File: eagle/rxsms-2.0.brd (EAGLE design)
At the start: 160 x 100 mm, 147 parts, among them Q1 opt, Q10 BSS123, Q11 BSS123, Q12 BSS123, Q2 BSS123, Q3 BSS123, Q4 BSS123, Q5 BSS123, Q6 BSS123, Q7 BSS123, Q8 BSS123, Q9 BSS123, T1 SMS_IP67, T10 SWITCH_LED, T2 SMS_IP67, T3 SWITCH_LED, T4 SMS_IP67, T5 SMS_IP67, T6 SWITCH_LED, T7 SWITCH_LED, T8 SWITCH_LED, T9 SMS_IP67, U1 MAX3232ESE, U2 XMEGA-A4UTQFP, U3 TSR_1-2450, U4 LM1117, U5 TMV_0505EN, U6 ADUM3160, U7 TPS73125, U8 NUP2202W1, X1 PN61729-S, X5 RLP2-200-500

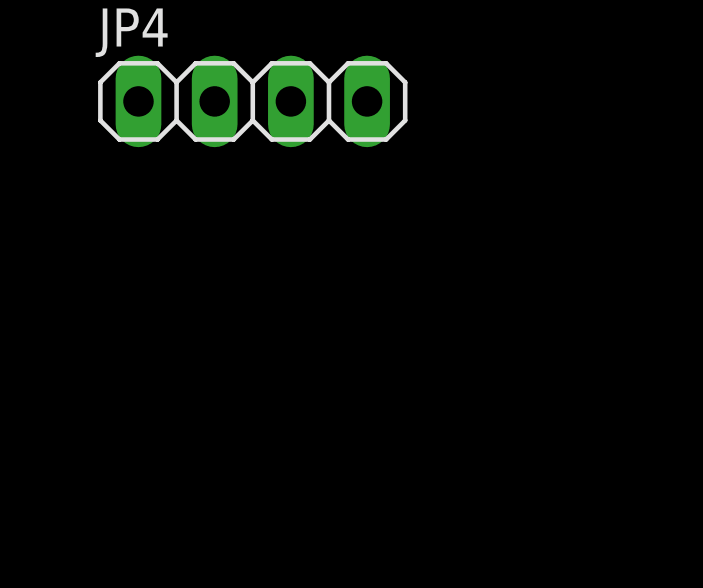
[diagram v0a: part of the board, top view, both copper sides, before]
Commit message: add pinheaders for reserved ADC and GPIO pins
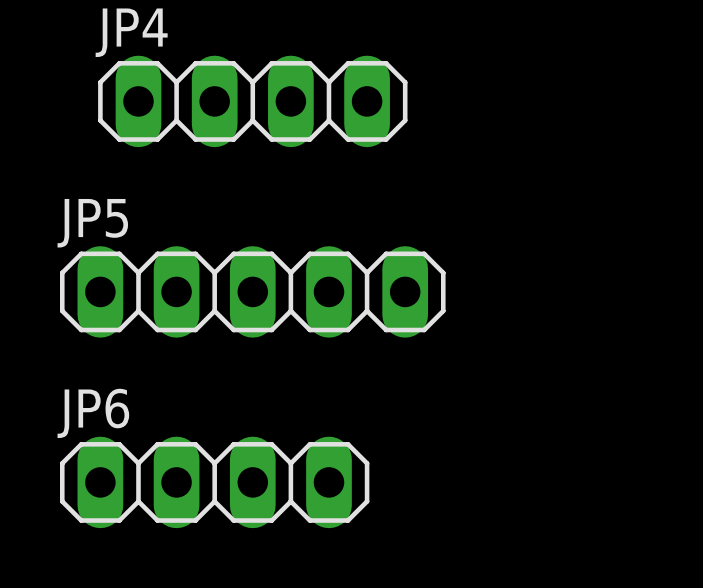
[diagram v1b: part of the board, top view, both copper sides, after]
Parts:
- added JP5: (no value), pinhead:1X05
- added JP6: (no value), pinhead:1X04
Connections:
- new net N$33: JP6.2, U2.28
- new net N$36: JP6.3, U2.29
- new net RESERVED_ADC_0: U2.44
- new net RESERVED_ADC_1: U2.1
- net +3V3: now also JP5.1, JP6.1
- net GND: now also JP5.5, JP6.4
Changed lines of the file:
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@@
 <element name="JP3" library="pinhead" package="1X04" value="" x="-420.37" y="-471.17"/>
 <element name="JP4" library="pinhead" package="1X04" value="" x="-420.37" y="-477.52"/>
+<element name="JP5" library="pinhead" package="1X05" value="" x="-420.37" y="-483.87"/>
+<element name="JP6" library="pinhead" package="1X04" value="" x="-421.64" y="-490.22"/>
 </elements>
 <signals>
@@
 <contactref element="JP3" pad="4"/>
 <contactref element="JP4" pad="4"/>
-<wire x1="-282.21" y1="-298.45" x2="-287.29" y2="-298.45" width="0" layer="19" extent="1-1"/>
-<wire x1="-266.7" y1="-293.37" x2="-282.21" y2="-298.45" width="0" layer="19" extent="1-1"/>
-<wire x1="-266.7" y1="-290.83" x2="-266.7" y2="-293.37" width="0" layer="19" extent="1-1"/>
-<wire x1="-266.7" y1="-281.94" x2="-266.7" y2="-290.83" width="0" layer="19" extent="1-1"/>
-<wire x1="-287.075" y1="-272.63" x2="-266.7" y2="-281.94" width="0" layer="19" extent="1-1"/>
-<wire x1="-287.075" y1="-258.43" x2="-287.075" y2="-272.63" width="0" layer="19" extent="1-1"/>
-<wire x1="-266.7" y1="-254" x2="-287.075" y2="-258.43" width="0" layer="19" extent="1-1"/>
-<wire x1="-266.7" y1="-251.46" x2="-266.7" y2="-254" width="0" layer="19" extent="1-1"/>
-<wire x1="-266.7" y1="-242.57" x2="-266.7" y2="-251.46" width="0" layer="19" extent="1-1"/>
-<wire x1="-266.7" y1="-240.03" x2="-266.7" y2="-242.57" width="0" layer="19" extent="1-1"/>
+<contactref element="JP5" pad="5"/>
+<contactref element="JP6" pad="4"/>
+<wire x1="-266.7" y1="-242.57" x2="-266.7" y2="-240.03" width="0" layer="19" extent="1-1"/>
+<wire x1="-266.7" y1="-251.46" x2="-266.7" y2="-242.57" width="0" layer="19" extent="1-1"/>
+<wire x1="-266.7" y1="-254" x2="-266.7" y2="-251.46" width="0" layer="19" extent="1-1"/>
+<wire x1="-287.075" y1="-258.43" x2="-266.7" y2="-254" width="0" layer="19" extent="1-1"/>
+<wire x1="-287.075" y1="-272.63" x2="-287.075" y2="-258.43" width="0" layer="19" extent="1-1"/>
+<wire x1="-266.7" y1="-281.94" x2="-287.075" y2="-272.63" width="0" layer="19" extent="1-1"/>
+<wire x1="-266.7" y1="-290.83" x2="-266.7" y2="-281.94" width="0" layer="19" extent="1-1"/>
+<wire x1="-266.7" y1="-293.37" x2="-266.7" y2="-290.83" width="0" layer="19" extent="1-1"/>
+<wire x1="-282.21" y1="-298.45" x2="-266.7" y2="-293.37" width="0" layer="19" extent="1-1"/>
+<wire x1="-287.29" y1="-298.45" x2="-282.21" y2="-298.45" width="0" layer="19" extent="1-1"/>
 <wire x1="-283.972" y1="-222.25" x2="-266.7" y2="-240.03" width="0" layer="19" extent="1-1"/>
 <wire x1="-266.7" y1="-327.66" x2="-282.21" y2="-298.45" width="0" layer="19" extent="1-1"/>
@@
 <wire x1="-416.56" y1="-471.17" x2="-408.62" y2="-463.55" width="0" layer="19" extent="1-1"/>
 <wire x1="-416.56" y1="-477.52" x2="-416.56" y2="-471.17" width="0" layer="19" extent="1-1"/>
+<wire x1="-415.29" y1="-483.87" x2="-416.56" y2="-477.52" width="0" layer="19" extent="1-1"/>
+<wire x1="-417.83" y1="-490.22" x2="-415.29" y2="-483.87" width="0" layer="19" extent="1-1"/>
 <wire x1="-280.035" y1="-167.1066" x2="-283.972" y2="-222.25" width="0" layer="19" extent="1-1"/>
 <wire x1="-280.035" y1="-118.8466" x2="-280.035" y2="-167.1066" width="0" layer="19" extent="1-1"/>
@@
 <wire x1="-178.07" y1="153.67" x2="-190.24" y2="139.98" width="0" layer="19" extent="1-1"/>
 <wire x1="-178.07" y1="158.75" x2="-178.07" y2="153.67" width="0" layer="19" extent="1-1"/>
-<wire x1="-169.545" y1="-221.46" x2="-178.07" y2="158.75" width="0" layer="19" extent="1-1"/>
+<wire x1="-169.545" y1="-221.46" x2="-266.7" y2="-240.03" width="0" layer="19" extent="1-1"/>
 <wire x1="-164.465" y1="-221.46" x2="-169.545" y2="-221.46" width="0" layer="19" extent="1-1"/>
 <wire x1="-129.81" y1="-194.31" x2="-164.465" y2="-221.46" width="0" layer="19" extent="1-1"/>
@@
 <contactref element="JP3" pad="1"/>
 <contactref element="JP4" pad="1"/>
+<contactref element="JP5" pad="1"/>
+<contactref element="JP6" pad="1"/>
 <wire x1="-122.24" y1="-156.21" x2="-105.41" y2="-134.62" width="0" layer="19" extent="1-1"/>
 <wire x1="-122.24" y1="-162.56" x2="-122.24" y2="-156.21" width="0" layer="19" extent="1-1"/>
@@
 <wire x1="-89.23" y1="28.66" x2="-93.43" y2="20.46" width="0" layer="19" extent="1-1"/>
 <wire x1="-81.83" y1="25.26" x2="-89.23" y2="28.66" width="0" layer="19" extent="1-1"/>
-<wire x1="-180.07" y1="158.75" x2="-170.815" y2="-221.46" width="0" layer="19" extent="1-1"/>
-<wire x1="-180.07" y1="153.67" x2="-180.07" y2="158.75" width="0" layer="19" extent="1-1"/>
-<wire x1="-187.96" y1="147.28" x2="-180.07" y2="153.67" width="0" layer="19" extent="1-1"/>
-<wire x1="-273.37" y1="-82.55" x2="-187.96" y2="147.28" width="0" layer="19" extent="1-1"/>
-<wire x1="-273.37" y1="-88.9" x2="-273.37" y2="-82.55" width="0" layer="19" extent="1-1"/>
-<wire x1="-265.75" y1="-114.3" x2="-273.37" y2="-88.9" width="0" layer="19" extent="1-1"/>
-<wire x1="-273.37" y1="-123.19" x2="-265.75" y2="-114.3" width="0" layer="19" extent="1-1"/>
-<wire x1="-282.575" y1="-118.8466" x2="-273.37" y2="-123.19" width="0" layer="19" extent="1-1"/>
-<wire x1="-283.845" y1="-118.8466" x2="-282.575" y2="-118.8466" width="0" layer="19" extent="1-1"/>
-<wire x1="-283.53" y1="-129.54" x2="-283.845" y2="-118.8466" width="0" layer="19" extent="1-1"/>
-<wire x1="-283.845" y1="-167.1066" x2="-283.53" y2="-129.54" width="0" layer="19" extent="1-1"/>
-<wire x1="-282.575" y1="-167.1066" x2="-283.845" y2="-167.1066" width="0" layer="19" extent="1-1"/>
-<wire x1="-274.64" y1="-177.8" x2="-282.575" y2="-167.1066" width="0" layer="19" extent="1-1"/>
+<wire x1="-274.64" y1="-177.8" x2="-170.815" y2="-221.46" width="0" layer="19" extent="1-1"/>
+<wire x1="-282.575" y1="-167.1066" x2="-274.64" y2="-177.8" width="0" layer="19" extent="1-1"/>
+<wire x1="-283.845" y1="-167.1066" x2="-282.575" y2="-167.1066" width="0" layer="19" extent="1-1"/>
+<wire x1="-283.53" y1="-129.54" x2="-282.575" y2="-167.1066" width="0" layer="19" extent="1-1"/>
+<wire x1="-283.845" y1="-118.8466" x2="-283.53" y2="-129.54" width="0" layer="19" extent="1-1"/>
+<wire x1="-282.575" y1="-118.8466" x2="-283.845" y2="-118.8466" width="0" layer="19" extent="1-1"/>
+<wire x1="-273.37" y1="-123.19" x2="-282.575" y2="-118.8466" width="0" layer="19" extent="1-1"/>
+<wire x1="-265.75" y1="-114.3" x2="-273.37" y2="-123.19" width="0" layer="19" extent="1-1"/>
+<wire x1="-273.37" y1="-88.9" x2="-265.75" y2="-114.3" width="0" layer="19" extent="1-1"/>
+<wire x1="-273.37" y1="-82.55" x2="-273.37" y2="-88.9" width="0" layer="19" extent="1-1"/>
+<wire x1="-187.96" y1="147.28" x2="-89.23" y2="28.66" width="0" layer="19" extent="1-1"/>
+<wire x1="-180.07" y1="153.67" x2="-187.96" y2="147.28" width="0" layer="19" extent="1-1"/>
+<wire x1="-180.07" y1="158.75" x2="-180.07" y2="153.67" width="0" layer="19" extent="1-1"/>
 <wire x1="-307.02" y1="-360.68" x2="-274.64" y2="-177.8" width="0" layer="19" extent="1-1"/>
 <wire x1="-305.12" y1="-381" x2="-307.02" y2="-360.68" width="0" layer="19" extent="1-1"/>
@@
 <wire x1="-424.18" y1="-471.17" x2="-305.12" y2="-393.7" width="0" layer="19" extent="1-1"/>
 <wire x1="-424.18" y1="-477.52" x2="-424.18" y2="-471.17" width="0" layer="19" extent="1-1"/>
+<wire x1="-425.45" y1="-483.87" x2="-424.18" y2="-477.52" width="0" layer="19" extent="1-1"/>
+<wire x1="-425.45" y1="-490.22" x2="-425.45" y2="-483.87" width="0" layer="19" extent="1-1"/>
 </signal>
 <signal name="N$11">
@@
 <contactref element="JP3" pad="3"/>
 </signal>
+<signal name="RESERVED_ADC_0">
+<contactref element="U2" pad="44"/>
+</signal>
+<signal name="RESERVED_ADC_1">
+<contactref element="U2" pad="1"/>
+</signal>
+<signal name="N$33">
+<contactref element="U2" pad="28"/>
+<contactref element="JP6" pad="2"/>
+<wire x1="-93.43" y1="22.86" x2="-422.91" y2="-490.22" width="0" layer="19" extent="1-1"/>
+</signal>
+<signal name="N$36">
+<contactref element="U2" pad="29"/>
+<contactref element="JP6" pad="3"/>
+<wire x1="-93.43" y1="22.06" x2="-420.37" y2="-490.22" width="0" layer="19" extent="1-1"/>
+</signal>
 </signals>

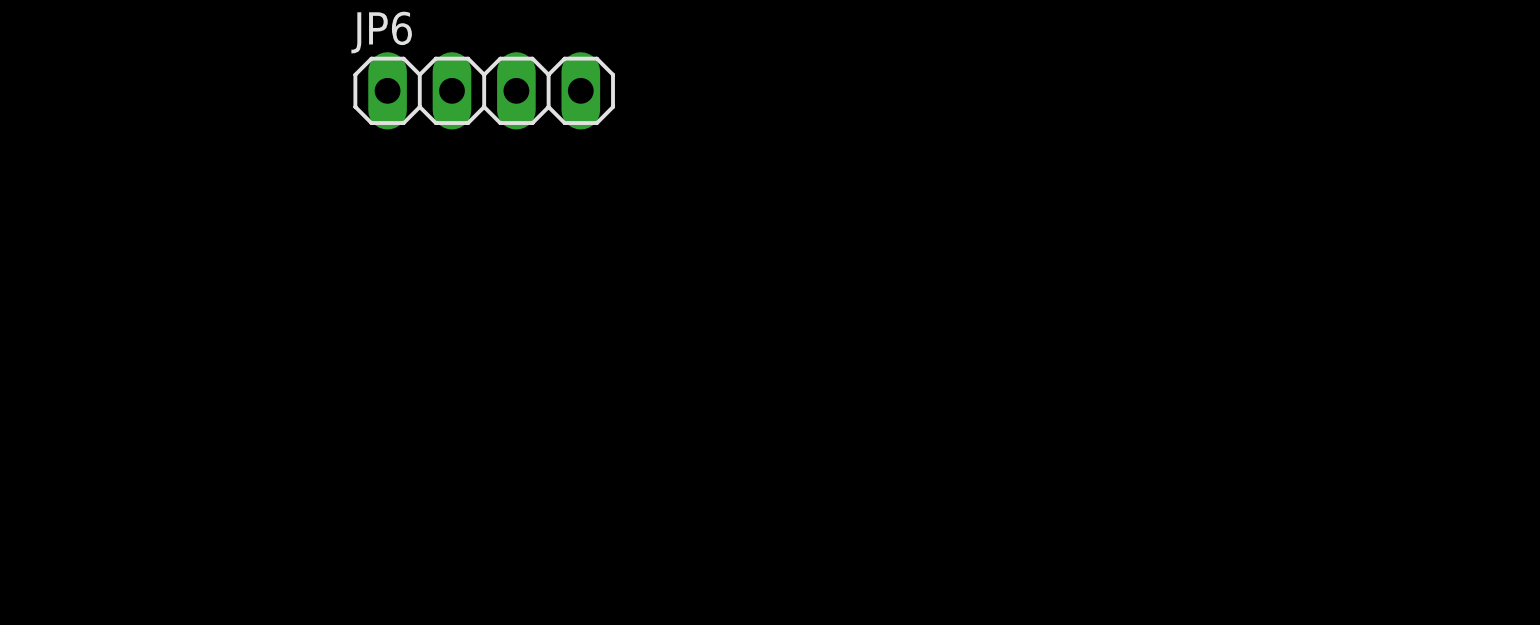
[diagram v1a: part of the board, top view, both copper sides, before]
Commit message: add power supply connectors
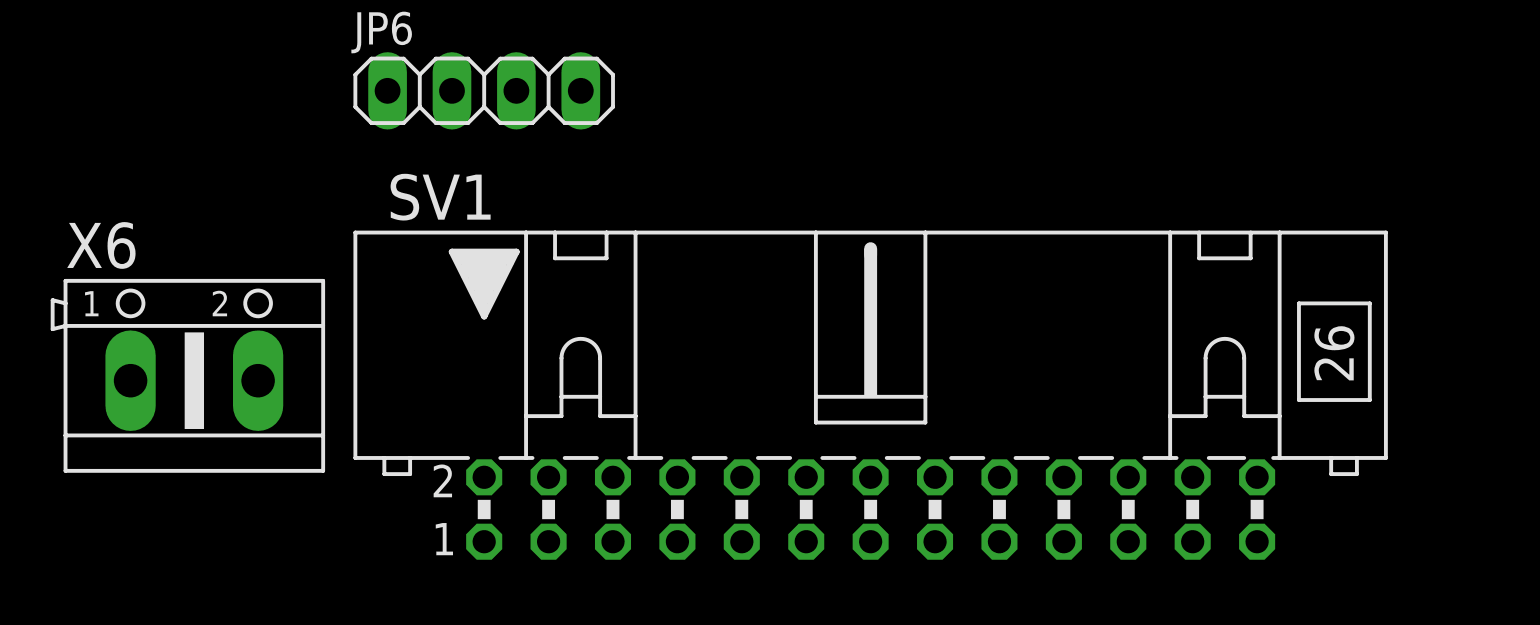
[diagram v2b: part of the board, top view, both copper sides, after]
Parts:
- added SV1: (no value), con-harting-ml:ML26L
- added X6: (no value), con-ptr500:AK500/2
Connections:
- new net N$67: SV1.10, SV1.12, SV1.14, SV1.4, SV1.6, SV1.8
- new net N$69: SV1.11, SV1.13, SV1.3, SV1.5, SV1.7, SV1.9
- net +28V_SUPPLY: now also SV1.15, SV1.16, SV1.17, SV1.18, SV1.19, SV1.20, SV1.21, SV1.22, SV1.23, SV1.24, SV1.25, SV1.26, X6.1
- net GND: now also X6.2
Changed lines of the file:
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@@
 <element name="JP5" library="pinhead" package="1X05" value="" x="-420.37" y="-483.87"/>
 <element name="JP6" library="pinhead" package="1X04" value="" x="-421.64" y="-490.22"/>
+<element name="SV1" library="con-harting-ml" package="ML26L" value="" x="-406.4" y="-506.73">
+<attribute name="OC_NEWARK" value="unknown" x="-406.4" y="-506.73" size="1.778" layer="27" display="off"/>
+<attribute name="MPN" value="" x="-406.4" y="-506.73" size="1.778" layer="27" display="off"/>
+<attribute name="MF" value="" x="-406.4" y="-506.73" size="1.778" layer="27" display="off"/>
+<attribute name="OC_FARNELL" value="unknown" x="-406.4" y="-506.73" size="1.778" layer="27" display="off"/>
+</element>
+<element name="X6" library="con-ptr500" package="AK500/2" value="" x="-433.07" y="-501.65">
+<attribute name="OC_NEWARK" value="unknown" x="-433.07" y="-501.65" size="1.778" layer="27" display="off"/>
+<attribute name="MPN" value="" x="-433.07" y="-501.65" size="1.778" layer="27" display="off"/>
+<attribute name="MF" value="" x="-433.07" y="-501.65" size="1.778" layer="27" display="off"/>
+<attribute name="OC_FARNELL" value="unknown" x="-433.07" y="-501.65" size="1.778" layer="27" display="off"/>
+</element>
 </elements>
 <signals>
@@
 <contactref element="JP5" pad="5"/>
 <contactref element="JP6" pad="4"/>
+<contactref element="X6" pad="2"/>
 <wire x1="-266.7" y1="-242.57" x2="-266.7" y2="-240.03" width="0" layer="19" extent="1-1"/>
 <wire x1="-266.7" y1="-251.46" x2="-266.7" y2="-242.57" width="0" layer="19" extent="1-1"/>
@@
 <wire x1="-415.29" y1="-483.87" x2="-416.56" y2="-477.52" width="0" layer="19" extent="1-1"/>
 <wire x1="-417.83" y1="-490.22" x2="-415.29" y2="-483.87" width="0" layer="19" extent="1-1"/>
+<wire x1="-430.5554" y1="-501.65" x2="-417.83" y2="-490.22" width="0" layer="19" extent="1-1"/>
 <wire x1="-280.035" y1="-167.1066" x2="-283.972" y2="-222.25" width="0" layer="19" extent="1-1"/>
 <wire x1="-280.035" y1="-118.8466" x2="-280.035" y2="-167.1066" width="0" layer="19" extent="1-1"/>
@@
 <contactref element="U$6" pad="TAB"/>
 <contactref element="C12" pad="1"/>
-<wire x1="-154.94" y1="-119.68" x2="-101.33" y2="-55.88" width="0" layer="19" extent="1-1"/>
+<contactref element="SV1" pad="16"/>
+<contactref element="SV1" pad="26"/>
+<contactref element="SV1" pad="18"/>
+<contactref element="SV1" pad="20"/>
+<contactref element="SV1" pad="22"/>
+<contactref element="SV1" pad="24"/>
+<contactref element="SV1" pad="25"/>
+<contactref element="SV1" pad="15"/>
+<contactref element="SV1" pad="17"/>
+<contactref element="SV1" pad="19"/>
+<contactref element="SV1" pad="21"/>
+<contactref element="SV1" pad="23"/>
+<contactref element="X6" pad="1"/>
+<wire x1="-403.86" y1="-505.46" x2="-435.5846" y2="-501.65" width="0" layer="19" extent="1-1"/>
+<wire x1="-403.86" y1="-508" x2="-403.86" y2="-505.46" width="0" layer="19" extent="1-1"/>
+<wire x1="-401.32" y1="-508" x2="-403.86" y2="-508" width="0" layer="19" extent="1-1"/>
+<wire x1="-401.32" y1="-505.46" x2="-403.86" y2="-505.46" width="0" layer="19" extent="1-1"/>
+<wire x1="-398.78" y1="-508" x2="-401.32" y2="-508" width="0" layer="19" extent="1-1"/>
+<wire x1="-398.78" y1="-505.46" x2="-401.32" y2="-505.46" width="0" layer="19" extent="1-1"/>
+<wire x1="-396.24" y1="-508" x2="-398.78" y2="-508" width="0" layer="19" extent="1-1"/>
+<wire x1="-396.24" y1="-505.46" x2="-398.78" y2="-505.46" width="0" layer="19" extent="1-1"/>
+<wire x1="-393.7" y1="-508" x2="-396.24" y2="-508" width="0" layer="19" extent="1-1"/>
+<wire x1="-393.7" y1="-505.46" x2="-396.24" y2="-505.46" width="0" layer="19" extent="1-1"/>
+<wire x1="-391.16" y1="-508" x2="-393.7" y2="-508" width="0" layer="19" extent="1-1"/>
+<wire x1="-391.16" y1="-505.46" x2="-393.7" y2="-505.46" width="0" layer="19" extent="1-1"/>
+<wire x1="-154.94" y1="-119.68" x2="-391.16" y2="-505.46" width="0" layer="19" extent="1-1"/>
+<wire x1="-101.33" y1="-55.88" x2="-154.94" y2="-119.68" width="0" layer="19" extent="1-1"/>
 </signal>
 <signal name="N$25">
@@
 <wire x1="-93.43" y1="22.06" x2="-420.37" y2="-490.22" width="0" layer="19" extent="1-1"/>
 </signal>
+<signal name="N$67">
+<contactref element="SV1" pad="4"/>
+<contactref element="SV1" pad="14"/>
+<contactref element="SV1" pad="12"/>
+<contactref element="SV1" pad="10"/>
+<contactref element="SV1" pad="8"/>
+<contactref element="SV1" pad="6"/>
+<wire x1="-416.56" y1="-505.46" x2="-419.1" y2="-505.46" width="0" layer="19" extent="1-1"/>
+<wire x1="-414.02" y1="-505.46" x2="-416.56" y2="-505.46" width="0" layer="19" extent="1-1"/>
+<wire x1="-411.48" y1="-505.46" x2="-414.02" y2="-505.46" width="0" layer="19" extent="1-1"/>
+<wire x1="-408.94" y1="-505.46" x2="-411.48" y2="-505.46" width="0" layer="19" extent="1-1"/>
+<wire x1="-406.4" y1="-505.46" x2="-408.94" y2="-505.46" width="0" layer="19" extent="1-1"/>
+</signal>
+<signal name="N$69">
+<contactref element="SV1" pad="13"/>
+<contactref element="SV1" pad="3"/>
+<contactref element="SV1" pad="5"/>
+<contactref element="SV1" pad="7"/>
+<contactref element="SV1" pad="9"/>
+<contactref element="SV1" pad="11"/>
+<wire x1="-416.56" y1="-508" x2="-419.1" y2="-508" width="0" layer="19" extent="1-1"/>
+<wire x1="-414.02" y1="-508" x2="-416.56" y2="-508" width="0" layer="19" extent="1-1"/>
+<wire x1="-411.48" y1="-508" x2="-414.02" y2="-508" width="0" layer="19" extent="1-1"/>
+<wire x1="-408.94" y1="-508" x2="-411.48" y2="-508" width="0" layer="19" extent="1-1"/>
+<wire x1="-406.4" y1="-508" x2="-408.94" y2="-508" width="0" layer="19" extent="1-1"/>
+</signal>
 </signals>

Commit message: most components selected
  * replaced unregulated TMV regulator with TES3
  * added coil library
  * added missing coils to DCDC regulators
  * added various 100nF capacitors
  * added jumper between USB shield and RC filter
  * operate MAX3232 at 3.3V and use matching capacitors
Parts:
- removed U5: TMV_0505EN, _traco_tmv-1:TMV-EN
- added C35: 4u7/50V, rcl:C0805K
- added C36, C37, C38, C39: 100n, rcl:C0805K
- added SJ4: (no value), jumper:SJ
- added U$10: TES3-4810WI, TES3-4810WI:TES3-4810WI
- added U$11, U$12: COIL, Coil:BOURNS-SRR0906
- C1, C2: value 470n -> 1u
- C3, C4, C5: value 3u3 -> 1u
- C30, C31: value 10u/16V -> 4u7/50V; device rcl:C1206K -> rcl:C0805K
- moved C31 543.1 mm to (-436.9, -547.4)
- moved C30 533.7 mm to (-436.9, -532.1)
- moved LED3 1.27 mm to (-406.4, -450.9)
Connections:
- removed net +VIN: C31.1, U5.1
- new net N$70: C31.1, U$10.P22, U$10.P23, U$11.P1
- new net N$71: SJ4.2, X1.S1, X1.S2
- new net N$72: C34.2, R48.1, SJ4.1
- new net VI: C35.1, U$12.P1, U3.1
- net +28V_SUPPLY: now also C30.1, U$11.P4, U$12.P4
- net +3V3: now also C37.1
- net +5V: now also C36.1, C38.1; no longer C30.1
- net ADC_REF: now also C39.1
- net GND: now also C35.2, C36.2, C37.2, C38.2, C39.2, U$10.P2, U$10.P3; no longer U5.2
- net USB_SHIELD: no longer C34.2, R48.1, X1.S1, X1.S2
- net VDD: now also U$10.P14; no longer U5.5
- net VSS: now also U$10.P16; no longer U5.7
